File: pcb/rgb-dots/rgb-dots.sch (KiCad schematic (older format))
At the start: 11 parts, among them J1 DATA IN, J2 5V IN, J3 GND IN, J4 5V OUT, J5 GND OUT, J6 DATA OUT, U1 WS2812B, U2 WS2812B

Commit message: Replaced RGB leds with IN-PI554FCH instead of WS2812B
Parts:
- C1, C2: symbol CAP -> passive:CAP
- H1: symbol Hole -> connectors:Hole
- J1, J2, J3, J4, J5, J6: symbol HEADER-1x01 -> connectors:HEADER-1x01
- U1, U2: value WS2812B -> IN-PI554FCH; symbol WS2812B -> opto:WS2812B
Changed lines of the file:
@@
-EESchema Schematic File Version 2
-LIBS:connectors
-LIBS:ic-cpu
-LIBS:ic-power
-LIBS:ic-misc
-LIBS:ic-io
-LIBS:passive
-LIBS:power
-LIBS:switches
-LIBS:opto
+EESchema Schematic File Version 4
 LIBS:rgb-dots-cache
-EELAYER 25 0
+EELAYER 26 0
 EELAYER END
 $Descr USLetter 11000 8500
@@
 Sheet 1 1
 Title "Display - RGB dots"
-Date "2016-07-11"
+Date "2018-08-29"
 Rev "B"
 Comp ""
@@
 $EndDescr
 $Comp
-L WS2812B U1
+L opto:WS2812B U1
 U 1 1 56DFE375
 P 5450 3600
 F 0 "U1" H 5100 3900 60  0000 L BNB
-F 1 "WS2812B" H 5100 3300 40  0000 L TNN
+F 1 "IN-PI554FCH" H 5100 3300 40  0000 L TNN
 F 2 "SMT:LED-5050" H 5100 3225 40  0001 L TNN
 F 3 "" H 5100 3900 50  0000 C CNN
@@
 $EndComp
 $Comp
-L CAP C1
+L passive:CAP C1
 U 1 1 56DFE3DD
 P 4700 3000
@@
 $EndComp
 $Comp
-L +5V #PWR01
+L power:+5V #PWR01
 U 1 1 56DFE46E
 P 4900 2850
@@
 $EndComp
 $Comp
-L GND #PWR02
+L power:GND #PWR02
 U 1 1 56DFE491
 P 4500 3100
@@
 $EndComp
 Wire Wire Line
-	4900 2850 4900 3500
+	4900 2850 4900 3000
 Wire Wire Line
 	4900 3500 5000 3500
@@
 	4500 3000 4500 3100
 $Comp
-L GND #PWR03
+L power:GND #PWR03
 U 1 1 56DFEB14
 P 5950 4000
@@
 	6100 3500 6100 3750
 $Comp
-L WS2812B U2
+L opto:WS2812B U2
 U 1 1 56DFEC23
 P 6800 3600
 F 0 "U2" H 6450 3900 60  0000 L BNB
-F 1 "WS2812B" H 6450 3300 40  0000 L TNN
+F 1 "IN-PI554FCH" H 6450 3300 40  0000 L TNN
 F 2 "SMT:LED-5050" H 6450 3225 40  0001 L TNN
 F 3 "" H 6450 3900 50  0000 C CNN
@@
 $EndComp
 $Comp
-L CAP C2
+L passive:CAP C2
 U 1 1 56DFEC2B
 P 6050 3000
@@
 $EndComp
 $Comp
-L +5V #PWR04
+L power:+5V #PWR04
 U 1 1 56DFEC31
 P 6250 2850
@@
 $EndComp
 $Comp
-L GND #PWR05
+L power:GND #PWR05
 U 1 1 56DFEC37
 P 5850 3100
@@
 $EndComp
 Wire Wire Line
-	6250 2850 6250 3500
+	6250 2850 6250 3000
 Wire Wire Line
 	6250 3500 6350 3500
@@
 	5850 3000 5850 3100
 $Comp
-L GND #PWR06
+L power:GND #PWR06
 U 1 1 56DFEC43
 P 7300 4000
@@
 	6100 3750 6350 3750
 $Comp
-L HEADER-1x01 J2
+L connectors:HEADER-1x01 J2
 U 1 1 56DFF4A0
 P 4850 5350
@@
 $EndComp
 $Comp
-L HEADER-1x01 J3
+L connectors:HEADER-1x01 J3
 U 1 1 56DFF624
 P 4850 6000
@@
 $EndComp
 $Comp
-L HEADER-1x01 J4
+L connectors:HEADER-1x01 J4
 U 1 1 56DFF67C
 P 6050 5350
@@
 $EndComp
 $Comp
-L HEADER-1x01 J5
+L connectors:HEADER-1x01 J5
 U 1 1 56DFF703
 P 6050 6000
@@
 $EndComp
 Wire Wire Line
-	5000 5350 5900 5350
-Wire Wire Line
-	5000 6000 5900 6000
-$Comp
-L SUP_+5V #PWR07
+	5000 5350 5450 5350
+Wire Wire Line
+	5000 6000 5450 6000
+$Comp
+L power:SUP_+5V #PWR07
 U 1 1 56DFF7B3
 P 5450 5150
@@
 $EndComp
 $Comp
-L SUP_GND #PWR08
+L power:SUP_GND #PWR08
 U 1 1 56DFF7DB
 P 5450 6200
@@
 Connection ~ 5450 5350
 $Comp
-L HEADER-1x01 J1
+L connectors:HEADER-1x01 J1
 U 1 1 56DFF9FA
 P 4100 3750
@@
 $EndComp
 $Comp
-L HEADER-1x01 J6
+L connectors:HEADER-1x01 J6
 U 1 1 56DFFB18
 P 8050 3500
@@
 DIN
 $Comp
-L Hole H1
+L connectors:Hole H1
 U 1 1 56E07857
 P 7700 5450
@@
 $EndComp
 $Comp
-L GND #PWR09
+L power:GND #PWR09
 U 1 1 56E078B7
 P 7700 5700
@@
 Wire Wire Line
 	7200 3500 7900 3500
+Wire Wire Line
+	4900 3000 4900 3500
+Wire Wire Line
+	6250 3000 6250 3500
+Wire Wire Line
+	5450 6000 5900 6000
+Wire Wire Line
+	5450 5350 5900 5350
 $EndSCHEMATC

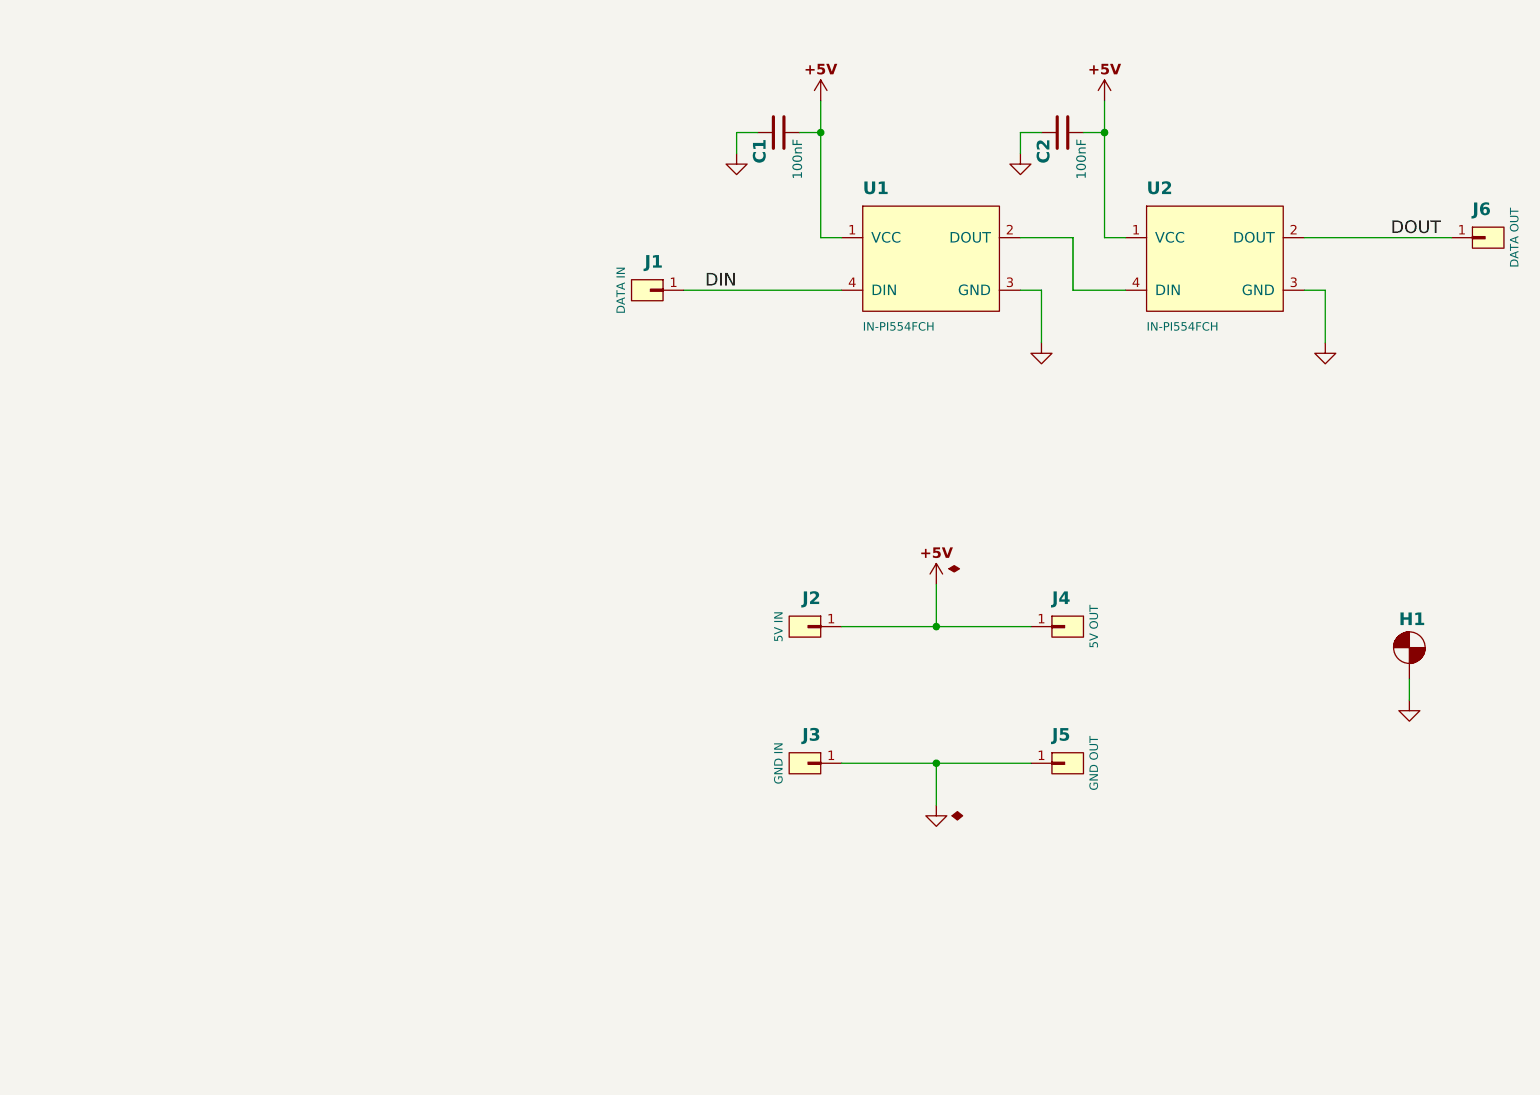
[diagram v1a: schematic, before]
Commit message: Updated PCB design
+ Completed daughterboard PCB layout.
* Corrected soldermask clerance on front panel pcb.
- Removed input resistor on DIN for RGB lamp board.
* Modified PCB layout for PSU board.
* Updated gerber files.
* Updated schematics pdf, BOM.
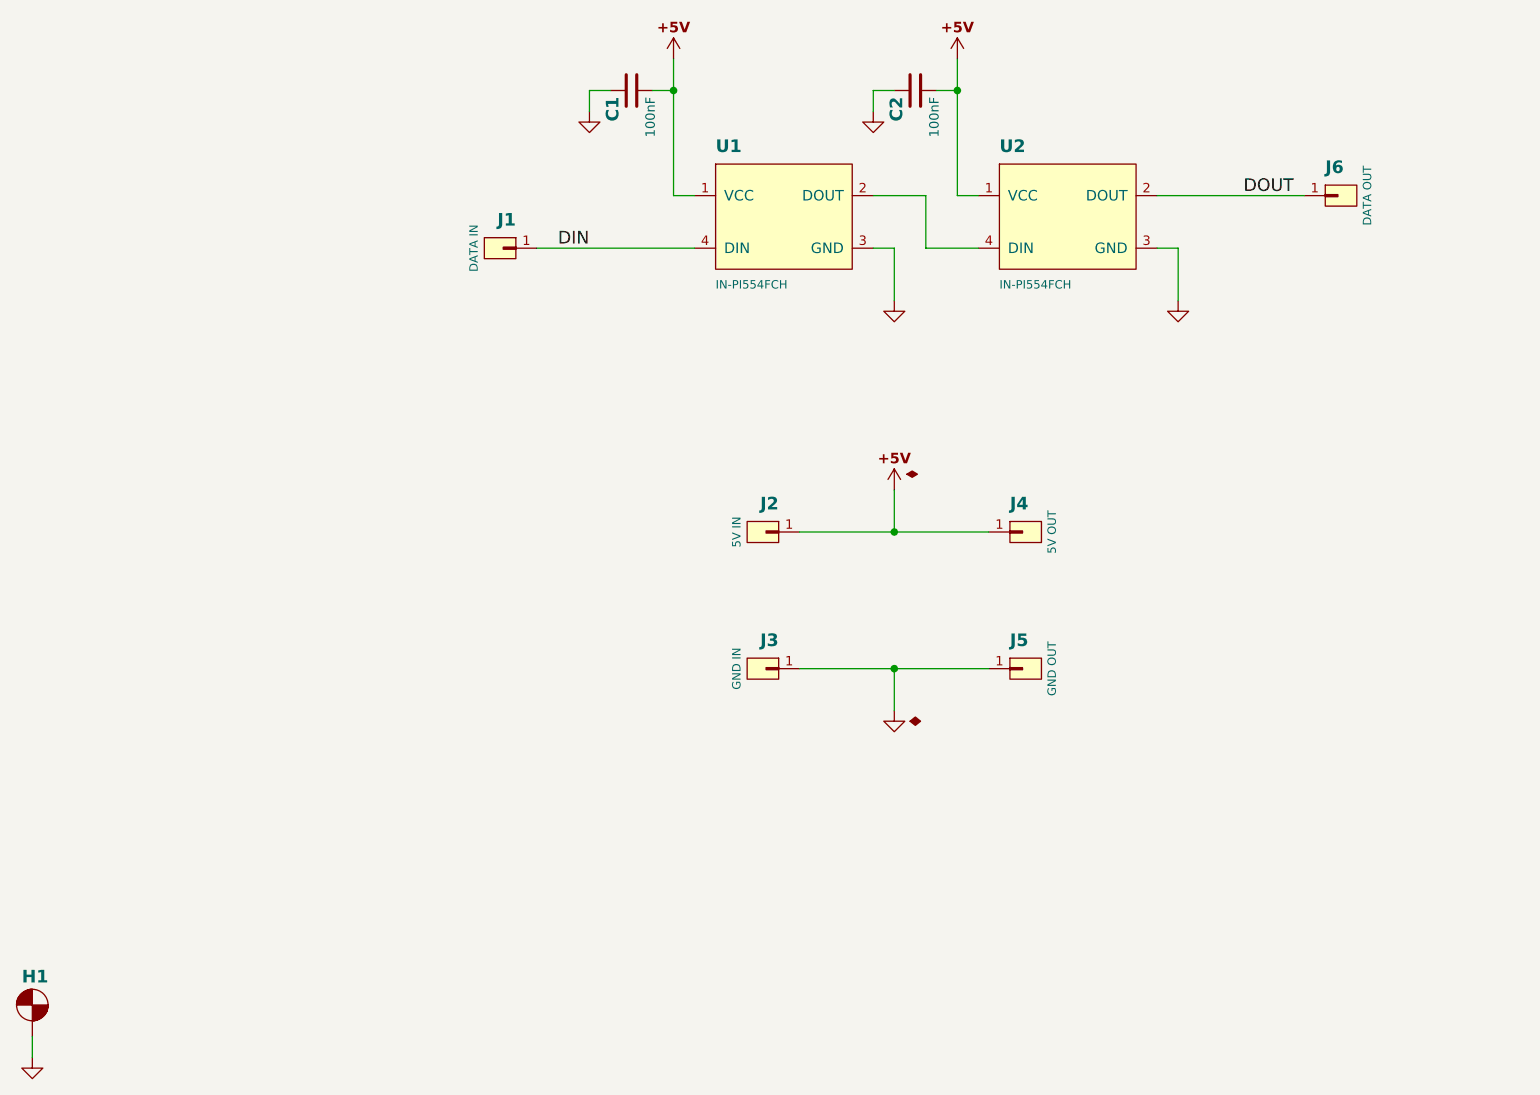
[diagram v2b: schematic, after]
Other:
- moved on the sheet: C1, C2, H1, J1, J2, J3, J4, J5, J6, U1, U2
